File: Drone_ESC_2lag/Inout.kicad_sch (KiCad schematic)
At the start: 13 parts, among them J1 Conn_02x05_Odd_Even, J2 Conn_01x02_Pin, J3 Conn_01x02_Pin, J4 Conn_01x03_Pin, P1 USB_C_Plug_USB2.0

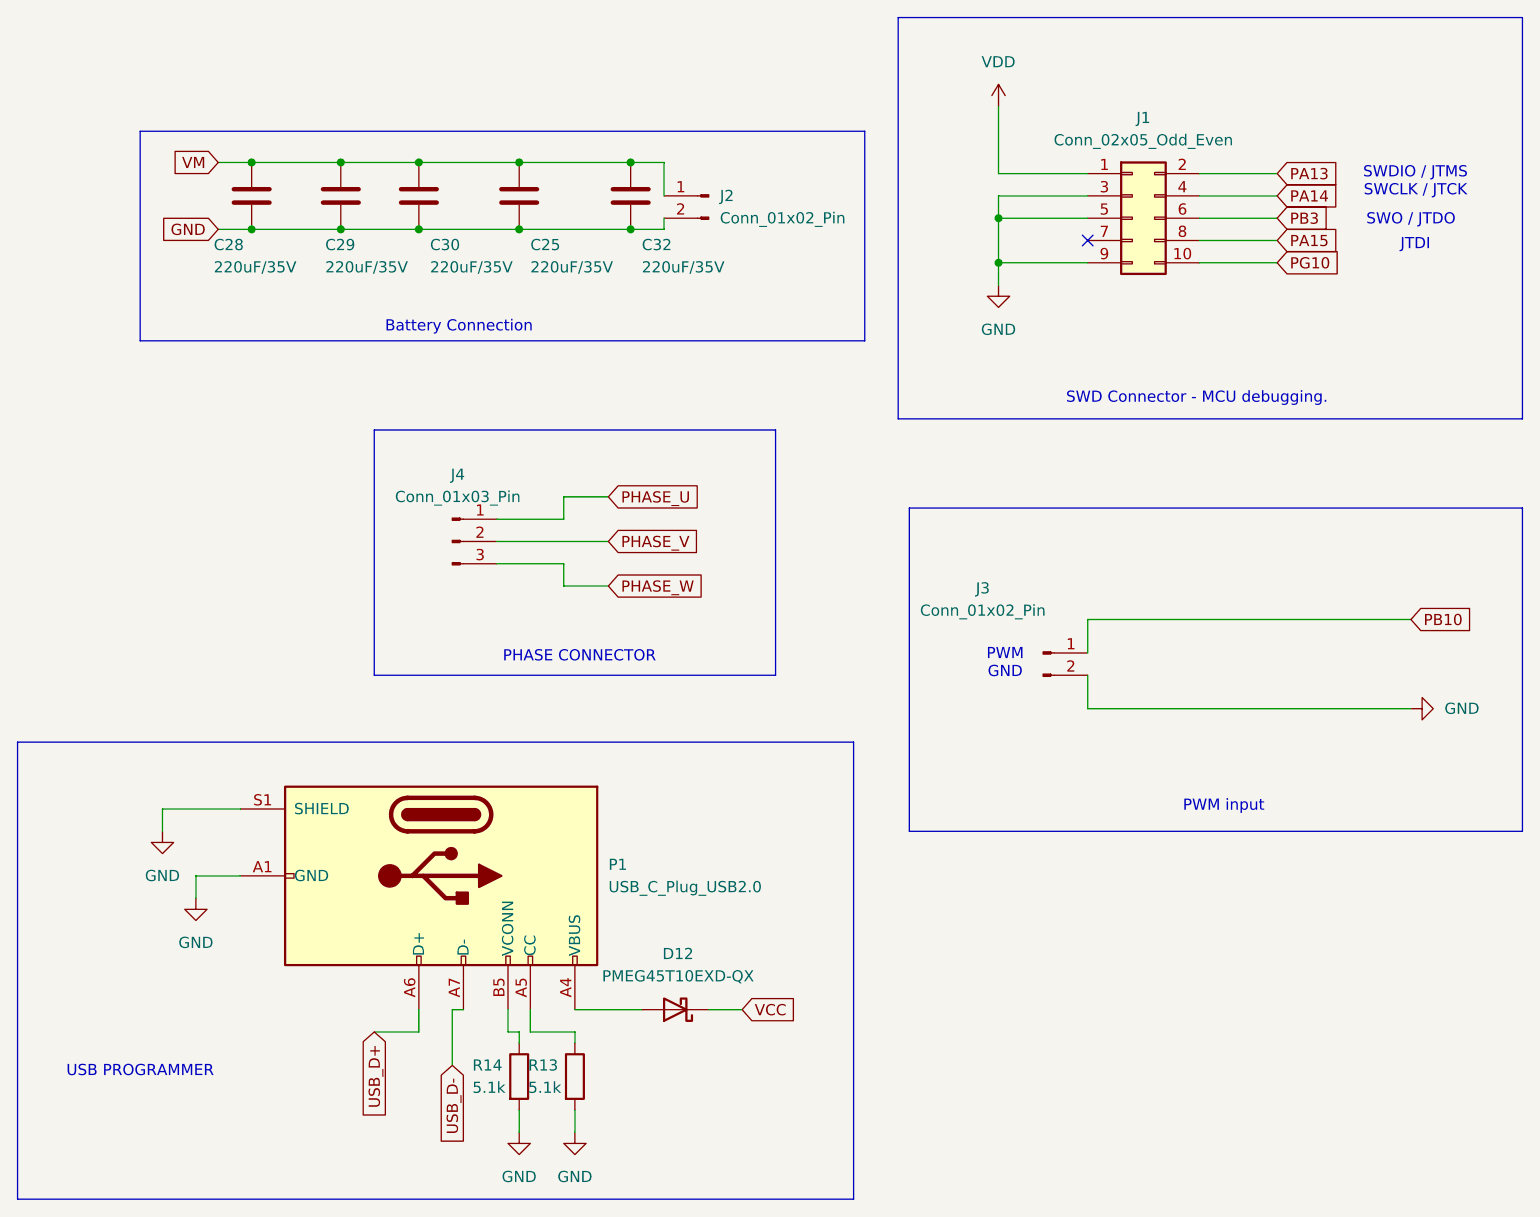
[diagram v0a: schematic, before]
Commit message: Næsten færdig med PCB, retter fejl
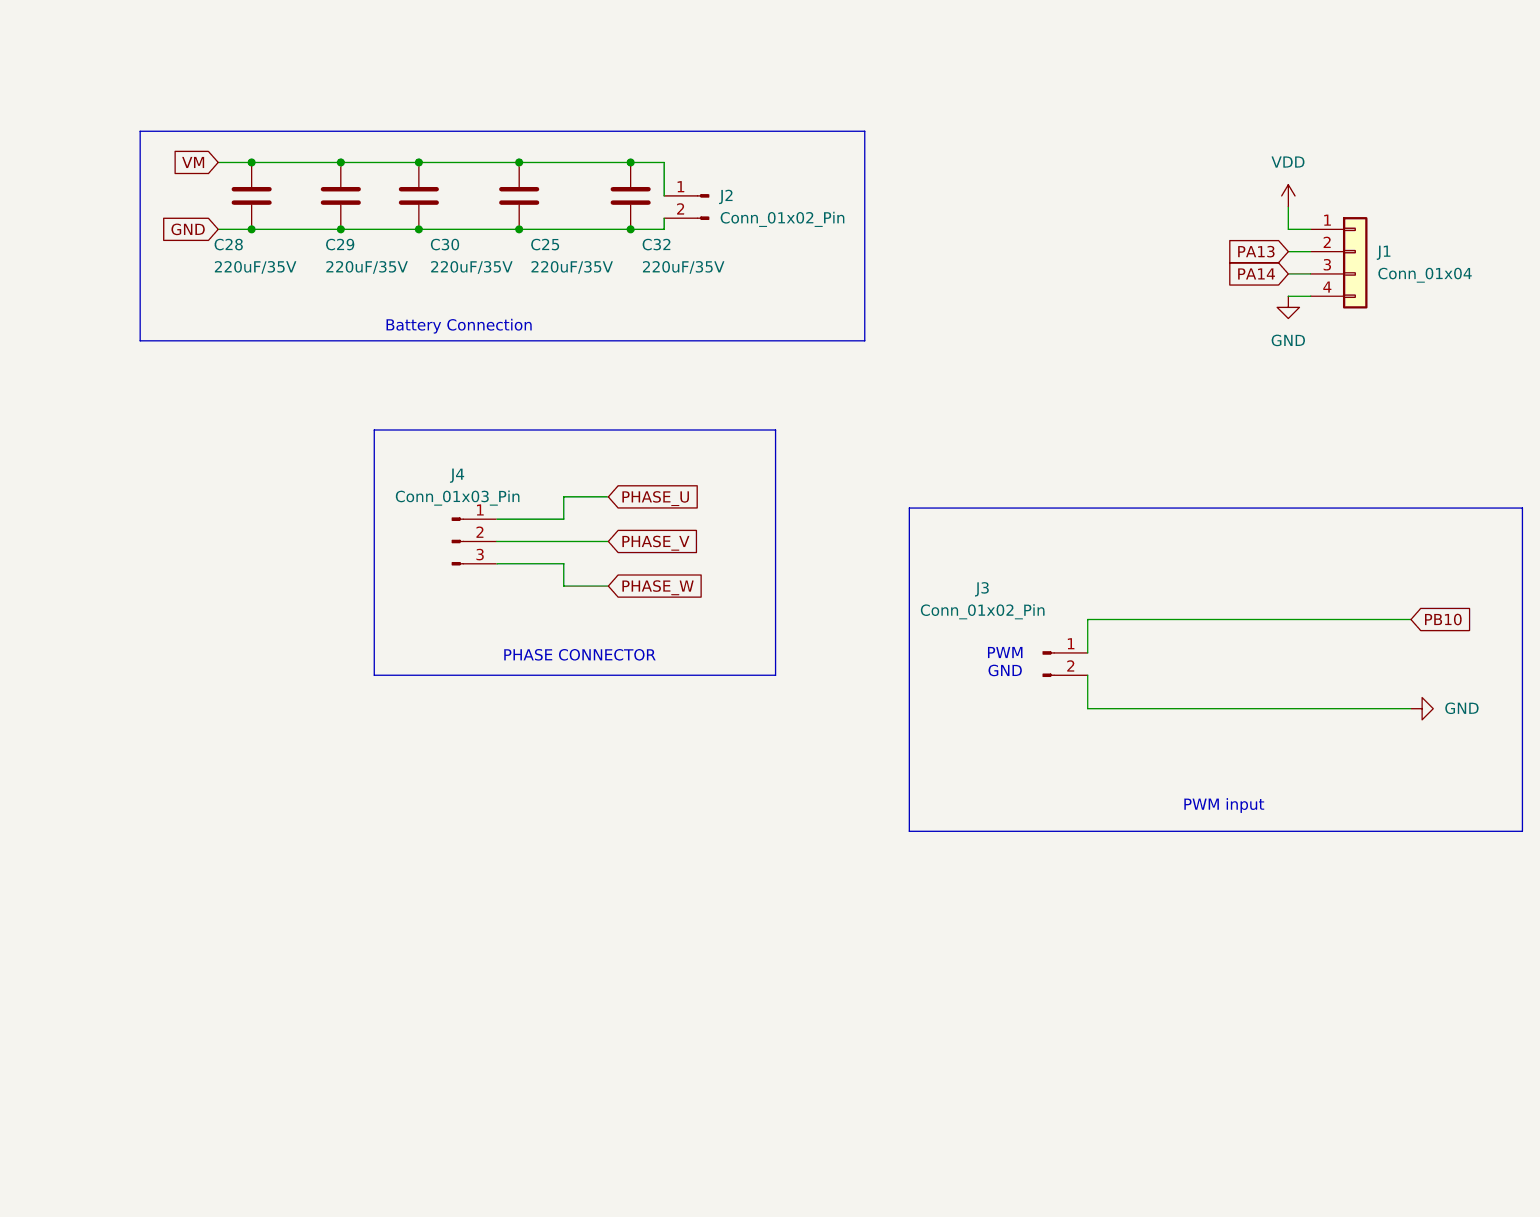
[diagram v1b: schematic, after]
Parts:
- removed D12: PMEG45T10EXD-QX, Diode_SMD:D_SOD-323_HandSoldering, symbol Device:D_Schottky
- removed J1: Conn_02x05_Odd_Even, Connector_PinHeader_1.27mm:PinHeader_2x05_P1.27mm_Vertical, symbol Connector_Generic:Conn_02x05_Odd_Even
- removed P1: USB_C_Plug_USB2.0, Connector_USB:USB_C_Receptacle_G-Switch_GT-USB-7010ASV, symbol Connector:USB_C_Plug_USB2.0
- removed R13, R14: 5.1k, Resistor_SMD:R_0805_2012Metric_Pad1.20x1.40mm_HandSolder, symbol Device:R
- added J1: Conn_01x04, Connector_PinHeader_2.54mm:PinHeader_1x04_P2.54mm_Vertical, symbol Connector_Generic:Conn_01x04
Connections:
- net GND: now also J1.4 (Pin_4)
- net PA13: now also J1.2 (Pin_2)
- net PA14: now also J1.3 (Pin_3)
- net VDD: now also J1.1 (Pin_1)
- no-connect marks 1 -> 0
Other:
- note removed: "SWD Connector - MCU debugging."
- note removed: "SWDIO / JTMS SWCLK / JTCK JTDI"
- note removed: "SWO / JTDO"
- note removed: "USB PROGRAMMER"
